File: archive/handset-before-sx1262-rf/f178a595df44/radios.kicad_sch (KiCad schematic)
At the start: 23 parts, among them J20 LORA_915_ANT, U36 0900FM15K0039001E, U37 BGS12WN6E6327, U4 SX1262IMLTRT, Y3 32MHz TCXO 0.5ppm temp

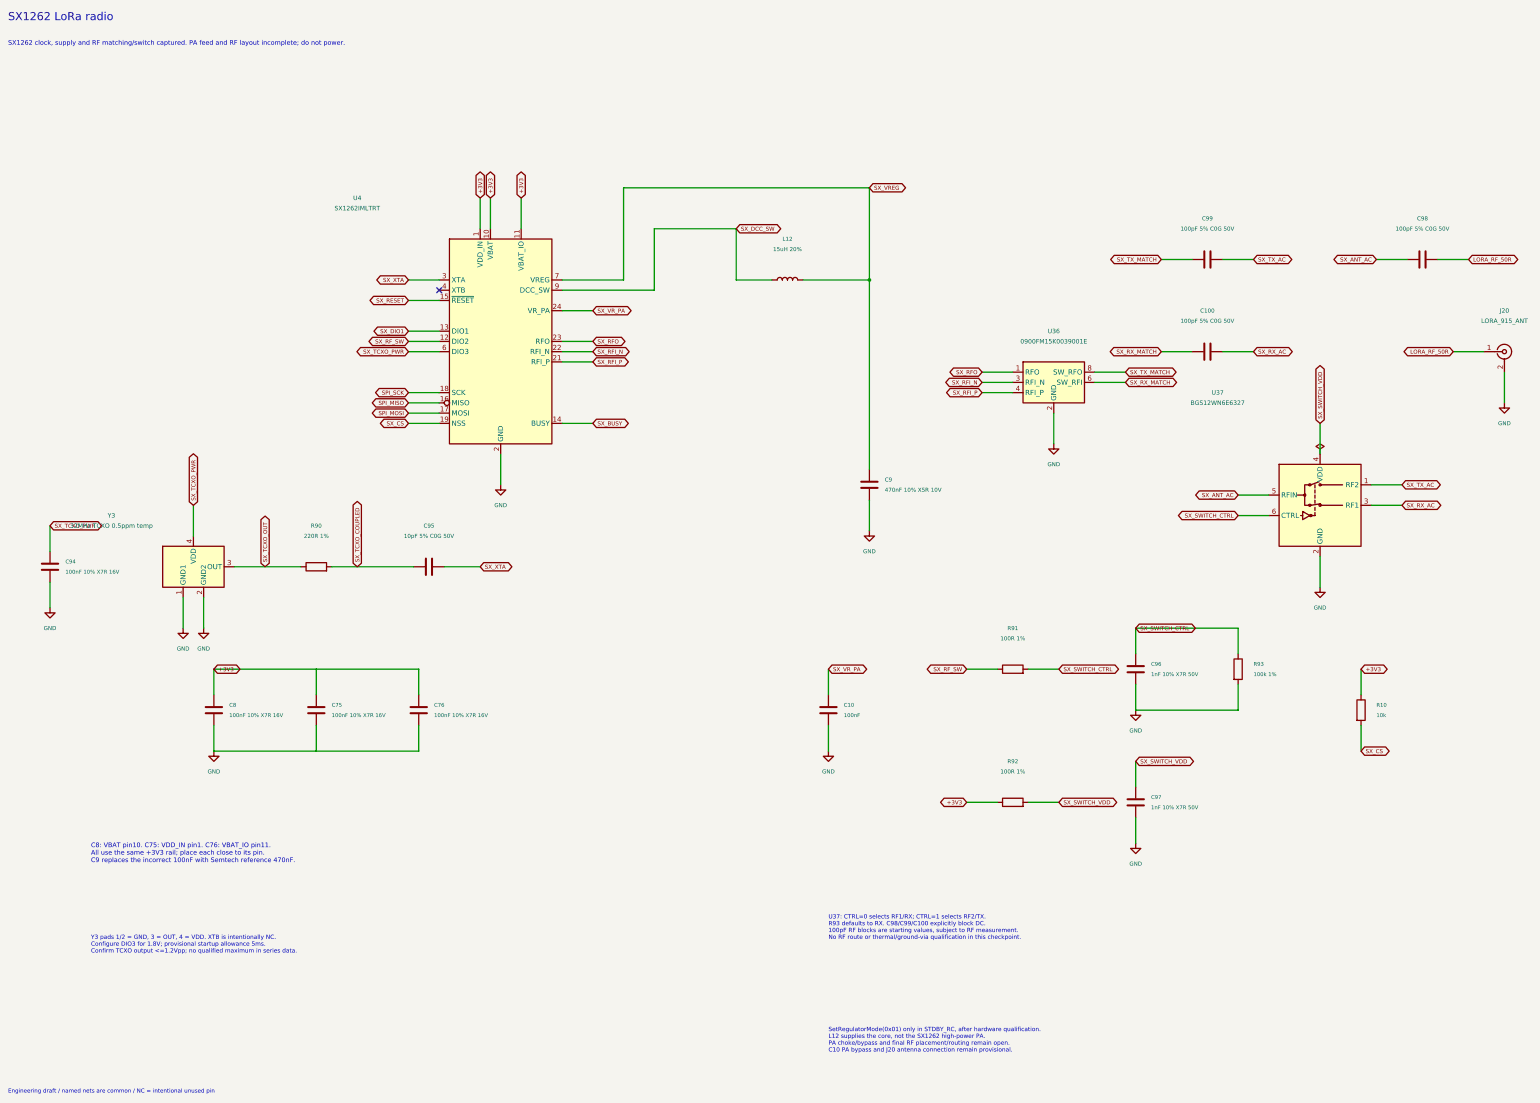
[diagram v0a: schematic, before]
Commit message: feat: capture SX1262 RF matching and switch
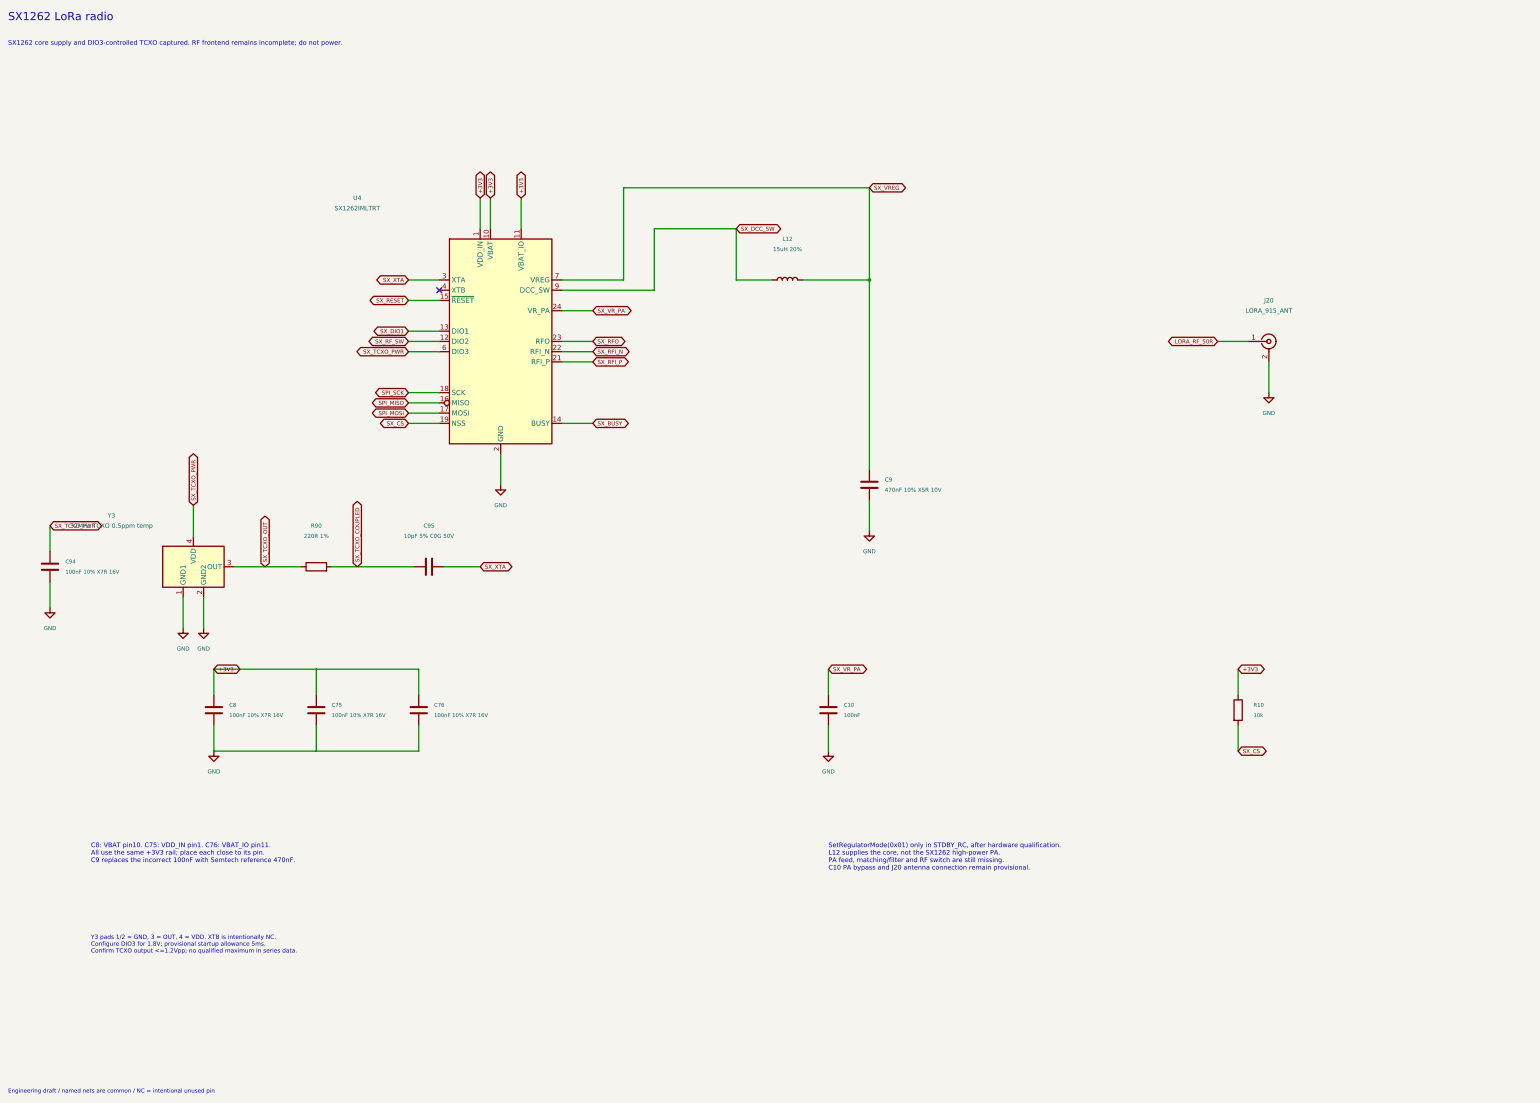
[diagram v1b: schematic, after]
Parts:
- removed C100, C98, C99: 100pF 5% C0G 50V, Capacitor_SMD:C_0402_1005Metric, symbol Device:C
- removed C96, C97: 1nF 10% X7R 50V, Capacitor_SMD:C_0402_1005Metric, symbol Device:C
- removed R91, R92: 100R 1%, Resistor_SMD:R_0402_1005Metric, symbol Device:R
- removed R93: 100k 1%, Resistor_SMD:R_0402_1005Metric, symbol Device:R
- removed U36: 0900FM15K0039001E, RF_Converter:Balun_Johanson_0900FM15K0039, symbol Filter:0900FM15K0039
- removed U37: BGS12WN6E6327, Package_LGA:Infineon_PG-TSNP-6-10_0.7x1.1mm_0.7x1.1mm_P0.4mm, symbol RF_Switch:BGS12WN6E6327
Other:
- note added: "SX1262 core supply and DIO3-controlled TCXO captured. RF frontend remains incomplete; do not power."
- note added: "SetRegulatorMode(0x01) only in STDBY_RC, after hardware qualification. L12 supplies the core, not the SX1262 high-power PA. PA feed, matching/filter and RF switch are still missing. C10 PA bypass and J20 antenna connection remain provisional."
- note removed: "SX1262 clock, supply and RF matching/switch captured. PA feed and RF layout incomplete; do not power."
- note removed: "SetRegulatorMode(0x01) only in STDBY_RC, after hardware qualification. L12 supplies the core, not the SX1262 high-power PA. PA choke/bypass and final RF placement/routing remain open. C10 PA bypass and J20 antenna connection remain provisional."
- note removed: "U37: CTRL=0 selects RF1/RX; CTRL=1 selects RF2/TX. R93 defaults to RX. C98/C99/C100 explicitly block DC. 100pF RF blocks are starting values, subject to RF measurement. No RF route or thermal/ground-via qualification in this checkpoint."
- moved on the sheet: J20, R10
